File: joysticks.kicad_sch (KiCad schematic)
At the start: 27 parts, among them J1 DB9_Male_MountingHoles, J2 DB9_Male_MountingHoles, J25 Joystick Ports Mezannine Lower, J26 Joystick Ports Mezannine Upper, SW1 Reset Button, U10 74LS06N, U11 74LS06N, U5 74LS06N, U6 74LVC374, U7 74LVC374, U8 74LS374, U9 74LS374

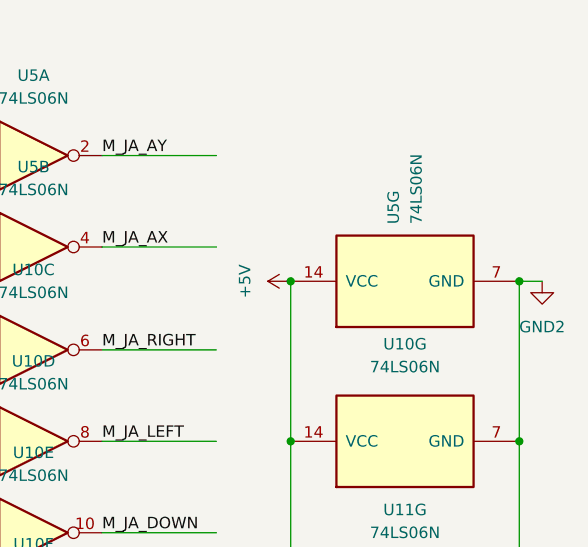
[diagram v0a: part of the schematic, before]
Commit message: re-do many labels and DRC fixes
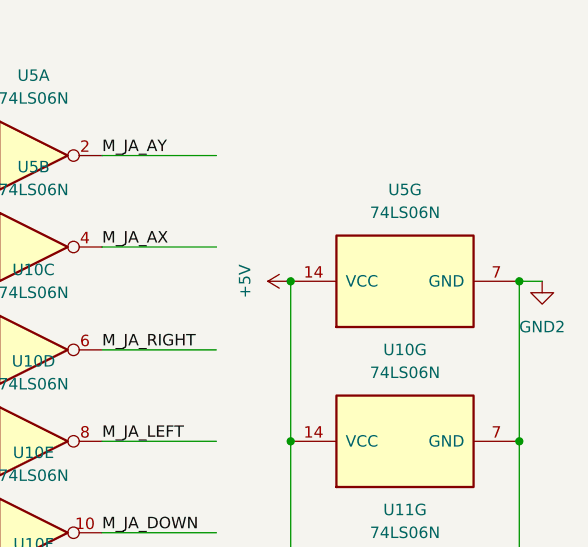
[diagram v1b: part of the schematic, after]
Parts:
- U10, U11, U5: footprint Package_DIP:DIP-14_W7.62mm -> snapeda:DIP-14_74LS06
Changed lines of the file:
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@@
     (property "Reference" "U5" (id 0) (at 223.52 19.05 0))
     (property "Value" "74LS06N" (id 1) (at 223.52 21.59 0))
-    (property "Footprint" "Package_DIP:DIP-14_W7.62mm" (id 2) (at 223.52 27.94 0)
+    (property "Footprint" "snapeda:DIP-14_74LS06" (id 2) (at 223.52 27.94 0)
       (effects (font (size 1.27 1.27)) hide)
     )
@@
     (property "Reference" "U10" (id 0) (at 223.52 101.6 0))
     (property "Value" "74LS06N" (id 1) (at 223.52 104.14 0))
-    (property "Footprint" "Package_DIP:DIP-14_W7.62mm" (id 2) (at 223.52 110.49 0)
+    (property "Footprint" "snapeda:DIP-14_74LS06" (id 2) (at 223.52 110.49 0)
       (effects (font (size 1.27 1.27)) hide)
     )
@@
     (property "Reference" "U5" (id 0) (at 191.77 149.225 0))
     (property "Value" "74LS06N" (id 1) (at 191.77 151.765 0))
-    (property "Footprint" "Package_DIP:DIP-14_W7.62mm" (id 2) (at 191.77 158.115 0)
+    (property "Footprint" "snapeda:DIP-14_74LS06" (id 2) (at 191.77 158.115 0)
       (effects (font (size 1.27 1.27)) hide)
     )
@@
     (property "Reference" "U10" (id 0) (at 223.52 60.96 0))
     (property "Value" "74LS06N" (id 1) (at 223.52 63.5 0))
-    (property "Footprint" "Package_DIP:DIP-14_W7.62mm" (id 2) (at 223.52 69.85 0)
+    (property "Footprint" "snapeda:DIP-14_74LS06" (id 2) (at 223.52 69.85 0)
       (effects (font (size 1.27 1.27)) hide)
     )
@@
   (symbol (lib_id "74xx:74LS06N") (at 264.795 41.91 90) (unit 7)
     (in_bom yes) (on_board yes) (fields_autoplaced)
-    (property "Reference" "U5" (id 0) (at 263.5249 35.56 0)
-      (effects (font (size 1.27 1.27)) (justify left))
-    )
-    (property "Value" "74LS06N" (id 1) (at 266.0649 35.56 0)
-      (effects (font (size 1.27 1.27)) (justify left))
-    )
-    (property "Footprint" "Package_DIP:DIP-14_W7.62mm" (id 2) (at 267.3349 35.56 0)
+    (property "Reference" "U5" (id 0) (at 264.795 31.75 90))
+    (property "Value" "74LS06N" (id 1) (at 264.795 34.29 90))
+    (property "Footprint" "snapeda:DIP-14_74LS06" (id 2) (at 267.3349 35.56 0)
       (effects (font (size 1.27 1.27)) (justify left) hide)
     )
@@
     (property "Reference" "U11" (id 0) (at 223.52 132.08 0))
     (property "Value" "74LS06N" (id 1) (at 223.52 134.62 0))
-    (property "Footprint" "Package_DIP:DIP-14_W7.62mm" (id 2) (at 223.52 140.97 0)
+    (property "Footprint" "snapeda:DIP-14_74LS06" (id 2) (at 223.52 140.97 0)
       (effects (font (size 1.27 1.27)) hide)
     )
@@
     (property "Reference" "U11" (id 0) (at 223.52 90.17 0))
     (property "Value" "74LS06N" (id 1) (at 223.52 92.71 0))
-    (property "Footprint" "Package_DIP:DIP-14_W7.62mm" (id 2) (at 223.52 99.06 0)
+    (property "Footprint" "snapeda:DIP-14_74LS06" (id 2) (at 223.52 99.06 0)
       (effects (font (size 1.27 1.27)) hide)
     )
@@
     (property "Reference" "U11" (id 0) (at 223.52 111.76 0))
     (property "Value" "74LS06N" (id 1) (at 223.52 114.3 0))
-    (property "Footprint" "Package_DIP:DIP-14_W7.62mm" (id 2) (at 223.52 120.65 0)
+    (property "Footprint" "snapeda:DIP-14_74LS06" (id 2) (at 223.52 120.65 0)
       (effects (font (size 1.27 1.27)) hide)
     )
@@
     (property "Reference" "U10" (id 0) (at 223.52 80.01 0))
     (property "Value" "74LS06N" (id 1) (at 223.52 82.55 0))
-    (property "Footprint" "Package_DIP:DIP-14_W7.62mm" (id 2) (at 223.52 88.9 0)
+    (property "Footprint" "snapeda:DIP-14_74LS06" (id 2) (at 223.52 88.9 0)
       (effects (font (size 1.27 1.27)) hide)
     )
@@
     (property "Reference" "U11" (id 0) (at 223.52 151.13 0))
     (property "Value" "74LS06N" (id 1) (at 223.52 153.67 0))
-    (property "Footprint" "Package_DIP:DIP-14_W7.62mm" (id 2) (at 223.52 160.02 0)
+    (property "Footprint" "snapeda:DIP-14_74LS06" (id 2) (at 223.52 160.02 0)
       (effects (font (size 1.27 1.27)) hide)
     )
@@
     (property "Reference" "U5" (id 0) (at 167.64 141.605 0))
     (property "Value" "74LS06N" (id 1) (at 167.64 144.145 0))
-    (property "Footprint" "Package_DIP:DIP-14_W7.62mm" (id 2) (at 167.64 150.495 0)
+    (property "Footprint" "snapeda:DIP-14_74LS06" (id 2) (at 167.64 150.495 0)
       (effects (font (size 1.27 1.27)) hide)
     )
@@
     (property "Reference" "U11" (id 0) (at 223.52 142.24 0))
     (property "Value" "74LS06N" (id 1) (at 223.52 144.78 0))
-    (property "Footprint" "Package_DIP:DIP-14_W7.62mm" (id 2) (at 223.52 151.13 0)
+    (property "Footprint" "snapeda:DIP-14_74LS06" (id 2) (at 223.52 151.13 0)
       (effects (font (size 1.27 1.27)) hide)
     )
@@
     (property "Reference" "U10" (id 0) (at 223.52 71.12 0))
     (property "Value" "74LS06N" (id 1) (at 223.52 73.66 0))
-    (property "Footprint" "Package_DIP:DIP-14_W7.62mm" (id 2) (at 223.52 80.01 0)
+    (property "Footprint" "snapeda:DIP-14_74LS06" (id 2) (at 223.52 80.01 0)
       (effects (font (size 1.27 1.27)) hide)
     )
@@
     (property "Reference" "U5" (id 0) (at 167.64 154.305 0))
     (property "Value" "74LS06N" (id 1) (at 167.64 156.845 0))
-    (property "Footprint" "Package_DIP:DIP-14_W7.62mm" (id 2) (at 167.64 163.195 0)
+    (property "Footprint" "snapeda:DIP-14_74LS06" (id 2) (at 167.64 163.195 0)
       (effects (font (size 1.27 1.27)) hide)
     )
@@
   (symbol (lib_id "74xx:74LS06N") (at 264.795 59.69 90) (unit 7)
     (in_bom yes) (on_board yes) (fields_autoplaced)
-    (property "Reference" "U10" (id 0) (at 264.795 48.895 90))
-    (property "Value" "74LS06N" (id 1) (at 264.795 51.435 90))
-    (property "Footprint" "Package_DIP:DIP-14_W7.62mm" (id 2) (at 264.795 59.69 0)
+    (property "Reference" "U10" (id 0) (at 264.795 49.53 90))
+    (property "Value" "74LS06N" (id 1) (at 264.795 52.07 90))
+    (property "Footprint" "snapeda:DIP-14_74LS06" (id 2) (at 264.795 59.69 0)
       (effects (font (size 1.27 1.27)) hide)
     )
@@
     (property "Reference" "U10" (id 0) (at 223.52 40.64 0))
     (property "Value" "74LS06N" (id 1) (at 223.52 43.18 0))
-    (property "Footprint" "Package_DIP:DIP-14_W7.62mm" (id 2) (at 223.52 49.53 0)
+    (property "Footprint" "snapeda:DIP-14_74LS06" (id 2) (at 223.52 49.53 0)
       (effects (font (size 1.27 1.27)) hide)
     )
@@
     (property "Reference" "U11" (id 0) (at 264.795 67.31 90))
     (property "Value" "74LS06N" (id 1) (at 264.795 69.85 90))
-    (property "Footprint" "Package_DIP:DIP-14_W7.62mm" (id 2) (at 264.795 77.47 0)
+    (property "Footprint" "snapeda:DIP-14_74LS06" (id 2) (at 264.795 77.47 0)
       (effects (font (size 1.27 1.27)) hide)
     )
@@
     (property "Reference" "U11" (id 0) (at 223.52 121.92 0))
     (property "Value" "74LS06N" (id 1) (at 223.52 124.46 0))
-    (property "Footprint" "Package_DIP:DIP-14_W7.62mm" (id 2) (at 223.52 130.81 0)
+    (property "Footprint" "snapeda:DIP-14_74LS06" (id 2) (at 223.52 130.81 0)
       (effects (font (size 1.27 1.27)) hide)
     )
@@
     (property "Reference" "U5" (id 0) (at 223.52 29.21 0))
     (property "Value" "74LS06N" (id 1) (at 223.52 31.75 0))
-    (property "Footprint" "Package_DIP:DIP-14_W7.62mm" (id 2) (at 223.52 38.1 0)
+    (property "Footprint" "snapeda:DIP-14_74LS06" (id 2) (at 223.52 38.1 0)
       (effects (font (size 1.27 1.27)) hide)
     )
@@
     (property "Reference" "U10" (id 0) (at 223.52 50.8 0))
     (property "Value" "74LS06N" (id 1) (at 223.52 53.34 0))
-    (property "Footprint" "Package_DIP:DIP-14_W7.62mm" (id 2) (at 223.52 59.69 0)
+    (property "Footprint" "snapeda:DIP-14_74LS06" (id 2) (at 223.52 59.69 0)
       (effects (font (size 1.27 1.27)) hide)
     )
@@
     (property "Reference" "U5" (id 0) (at 167.64 167.005 0))
     (property "Value" "74LS06N" (id 1) (at 167.64 169.545 0))
-    (property "Footprint" "Package_DIP:DIP-14_W7.62mm" (id 2) (at 167.64 175.895 0)
-      (effects (font (size 1.27 1.27)) hide)
-    )
+    (property "Footprint" "snapeda:DIP-14_74LS06" (id 2) (at 167.64 175.895 0)
+      (effects (font (size 1.27 1.27)) hide)
+    )
